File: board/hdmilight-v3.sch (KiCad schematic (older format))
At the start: 5 parts

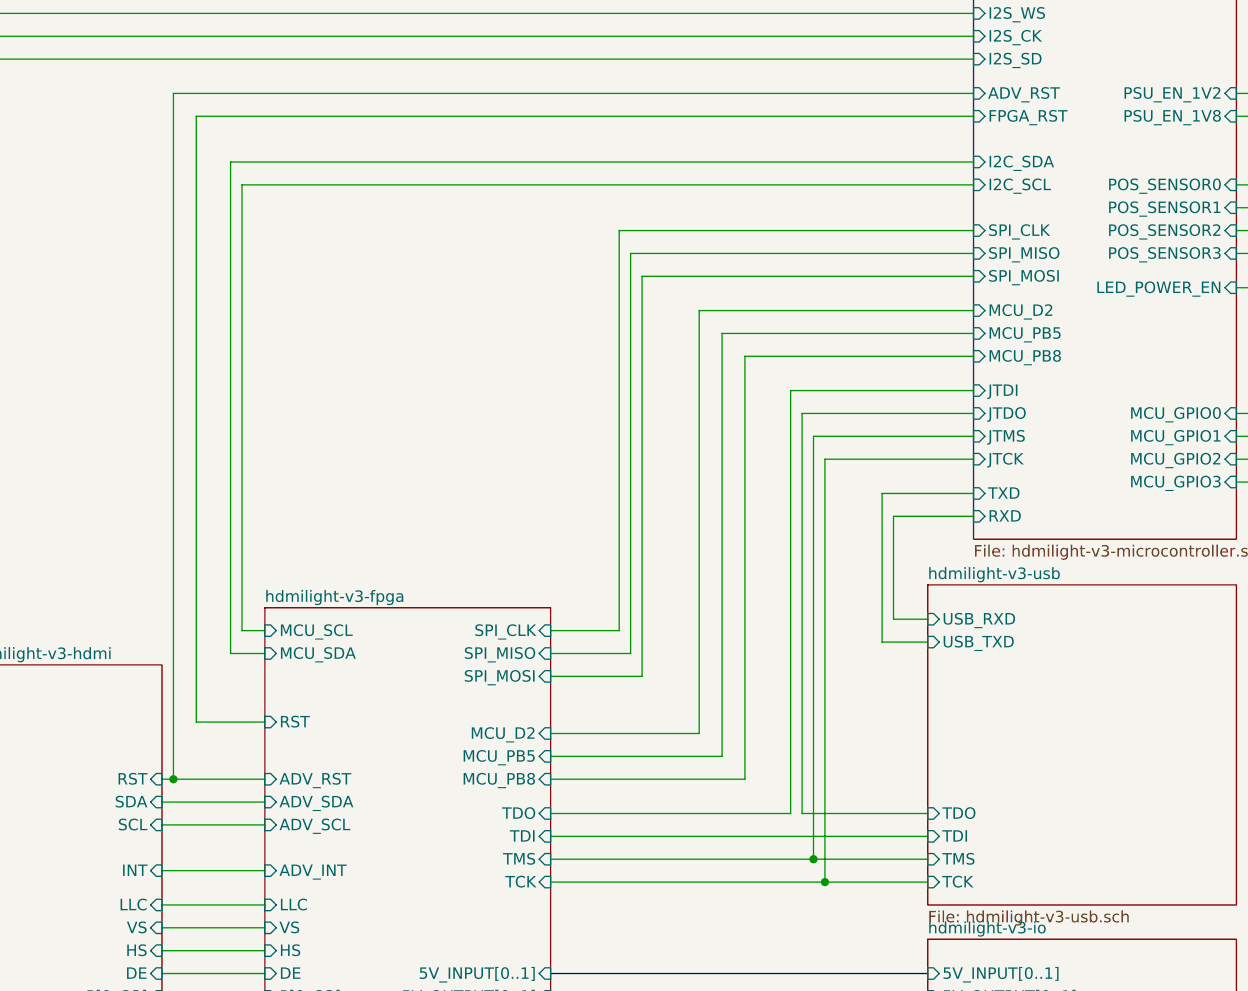
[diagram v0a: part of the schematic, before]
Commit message: Fixed bugs in v3.0 board:
 * Changed FPGA GPIO to 2 row with ground to make it compatible with logic analyser plug for debugging
 * Move position sensor from PB4 to PB5
 * Connect voltage regulator center pad to ground pins
 * Add SPI CS line between FPGA and MCU
 * Move HDMI hotplug LED back from board edge
 * Move HDMI ESD chip closer to connector
 * Swap serial rx/tx
 * Fix FPGA EEPROM footprint
 * Fix reset button footprint
 * Connect ADV I2C to MCU
 * Fix missing ground to hotplug power off circuit
 * Move LED power connector to back of board
 * Move standby button to front of board
 * Only use HDMI 5v for hotplug detect
 * Change LED power switching to high side to stop it grounding back through the data line
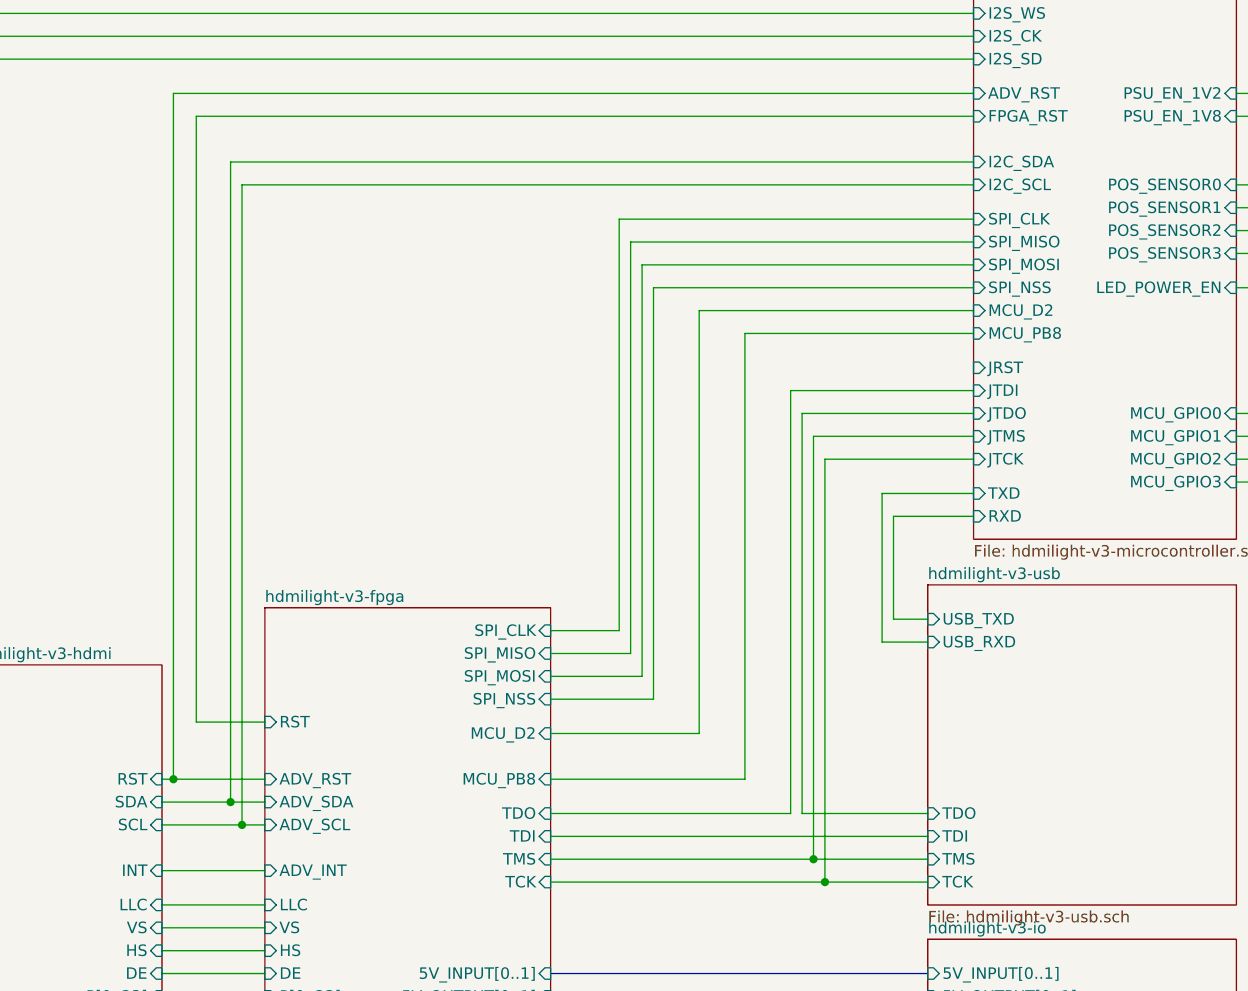
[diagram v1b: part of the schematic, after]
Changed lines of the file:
@@
 F26 "ADV_SCLK" I L 3550 5350 50
 F27 "ADV_AP" I L 3550 5450 50
-F28 "MCU_SDA" I L 3550 3450 50
-F29 "MCU_SCL" I L 3550 3350 50
-F30 "MCU_D2" I R 4800 3800 50
-F31 "MCU_PB5" I R 4800 3900 50
-F32 "MCU_PB8" I R 4800 4000 50
-F33 "RST" I L 3550 3750 50
-F34 "5V_OUTPUT[0..1]" I R 4800 4950 50
-F35 "PAPIX_POS[0..1]" I R 4800 5250 50
-F36 "FPGA_GPIO[0..7]" I R 4800 5350 50
-F37 "5V_INPUT[0..1]" I R 4800 4850 50
+F28 "MCU_D2" I R 4800 3800 50
+F29 "MCU_PB8" I R 4800 4000 50
+F30 "RST" I L 3550 3750 50
+F31 "5V_OUTPUT[0..1]" I R 4800 4950 50
+F32 "PAPIX_POS[0..1]" I R 4800 5250 50
+F33 "FPGA_GPIO[0..7]" I R 4800 5350 50
+F34 "5V_INPUT[0..1]" I R 4800 4850 50
+F35 "SPI_NSS" I R 4800 3650 50
 $EndSheet
 Wire Bus Line
@@
 F4 "JTDI" I L 6650 2300 50
 F5 "JTDO" I L 6650 2400 50
-F6 "SPI_CLK" I L 6650 1600 50
-F7 "SPI_MISO" I L 6650 1700 50
-F8 "SPI_MOSI" I L 6650 1800 50
+F6 "SPI_CLK" I L 6650 1550 50
+F7 "SPI_MISO" I L 6650 1650 50
+F8 "SPI_MOSI" I L 6650 1750 50
 F9 "I2C_SCL" I L 6650 1400 50
 F10 "I2C_SDA" I L 6650 1300 50
@@
 F17 "LED_POWER_EN" I R 7800 1850 50
 F18 "MCU_D2" I L 6650 1950 50
-F19 "MCU_PB5" I L 6650 2050 50
-F20 "MCU_PB8" I L 6650 2150 50
-F21 "ADV_RST" I L 6650 1000 50
-F22 "PSU_EN_1V2" I R 7800 1000 50
-F23 "PSU_EN_1V8" I R 7800 1100 50
-F24 "FPGA_RST" I L 6650 1100 50
-F25 "MCU_GPIO0" I R 7800 2400 50
-F26 "MCU_GPIO1" I R 7800 2500 50
-F27 "MCU_GPIO2" I R 7800 2600 50
-F28 "MCU_GPIO3" I R 7800 2700 50
-F29 "I2S_WS" I L 6650 650 50
-F30 "I2S_CK" I L 6650 750 50
-F31 "I2S_SD" I L 6650 850 50
+F19 "MCU_PB8" I L 6650 2050 50
+F20 "ADV_RST" I L 6650 1000 50
+F21 "PSU_EN_1V2" I R 7800 1000 50
+F22 "PSU_EN_1V8" I R 7800 1100 50
+F23 "FPGA_RST" I L 6650 1100 50
+F24 "MCU_GPIO0" I R 7800 2400 50
+F25 "MCU_GPIO1" I R 7800 2500 50
+F26 "MCU_GPIO2" I R 7800 2600 50
+F27 "MCU_GPIO3" I R 7800 2700 50
+F28 "I2S_WS" I L 6650 650 50
+F29 "I2S_CK" I L 6650 750 50
+F30 "I2S_SD" I L 6650 850 50
+F31 "SPI_NSS" I L 6650 1850 50
+F32 "JRST" I L 6650 2200 50
 $EndSheet
 Wire Wire Line
@@
 	3400 1300 6650 1300
 Wire Wire Line
-	3550 3350 3450 3350
-Wire Wire Line
-	3450 3350 3450 1400
-Wire Wire Line
 	3450 1400 6650 1400
 Wire Wire Line
 	4800 3350 5100 3350
 Wire Wire Line
-	5100 3350 5100 1600
-Wire Wire Line
-	5100 1600 6650 1600
+	5100 3350 5100 1550
+Wire Wire Line
+	5100 1550 6650 1550
 Wire Wire Line
 	4800 3450 5150 3450
 Wire Wire Line
-	5150 3450 5150 1700
-Wire Wire Line
-	5150 1700 6650 1700
+	5150 3450 5150 1650
+Wire Wire Line
+	5150 1650 6650 1650
 Wire Wire Line
 	4800 3550 5200 3550
 Wire Wire Line
-	5200 3550 5200 1800
-Wire Wire Line
-	5200 1800 6650 1800
+	5200 3550 5200 1750
+Wire Wire Line
+	5200 1750 6650 1750
 Wire Wire Line
 	7800 1700 8650 1700
@@
 $EndComp
 Wire Wire Line
-	3100 4100 3550 4100
-Wire Wire Line
-	3100 4200 3550 4200
+	3100 4100 3400 4100
+Wire Wire Line
+	3100 4200 3450 4200
 Wire Wire Line
 	3100 4400 3550 4400
@@
 	5450 1950 6650 1950
 Wire Wire Line
-	4800 3900 5550 3900
-Wire Wire Line
-	5550 3900 5550 2050
-Wire Wire Line
-	5550 2050 6650 2050
-Wire Wire Line
 	4800 4000 5650 4000
 Wire Wire Line
-	5650 4000 5650 2150
-Wire Wire Line
-	5650 2150 6650 2150
+	5650 4000 5650 2050
+Wire Wire Line
+	5650 2050 6650 2050
 Wire Wire Line
 	3150 4000 3150 1000
@@
 	3200 5900 3200 5450
 Wire Wire Line
-	3400 1300 3400 3450
-Wire Wire Line
-	3400 3450 3550 3450
-Wire Wire Line
 	6250 2750 6250 3400
 $Sheet
@@
 F0 "hdmilight-v3-usb" 50
 F1 "hdmilight-v3-usb.sch" 50
-F2 "USB_RXD" I L 6450 3300 50
-F3 "USB_TXD" I L 6450 3400 50
+F2 "USB_RXD" I L 6450 3400 50
+F3 "USB_TXD" I L 6450 3300 50
 F4 "TCK" I L 6450 4450 50
 F5 "TDI" I L 6450 4250 50
@@
 Wire Wire Line
 	5950 2500 5950 4350
+Wire Wire Line
+	6650 1850 5250 1850
+Wire Wire Line
+	5250 1850 5250 3650
+Wire Wire Line
+	5250 3650 4800 3650
+Wire Wire Line
+	3400 1300 3400 4100
+Connection ~ 3400 4100
+Wire Wire Line
+	3400 4100 3550 4100
+Wire Wire Line
+	3450 1400 3450 4200
+Connection ~ 3450 4200
+Wire Wire Line
+	3450 4200 3550 4200
 $EndSCHEMATC
